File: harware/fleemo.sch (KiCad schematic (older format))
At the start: 33 parts

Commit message: add value of the components
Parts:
- C1: renamed from C?; value C_Small -> 4.7uF
- C2, C3: renamed from C?; value CP1_Small -> 10uF
- C4, C5: renamed from C?; value C_Small -> 470pF
- C6: renamed from C?; value C_Small -> 1000pF
- C7: renamed from C?; value CP1_Small -> 820uF
- C8: renamed from C?; value CP1_Small -> 680uF
- C9: renamed from C?; value C_Small -> 0.1uF
- L1: renamed from L?; value L_Small -> 220uH
- R1: renamed from R?; value R_Small -> 68
- R10: renamed from R?; value R_Small -> 330K
- R11: renamed from R?; value R_Small -> 120
- R12: renamed from R?; value R_Small -> 2
- R13: renamed from R?; value R_Small -> 20
- R14: renamed from R?; value R_Small -> 2.4k
- R2: renamed from R?; value R_Small -> 47k
- R3: renamed from R?; value R_Small -> 300k
- R4, R7: renamed from R?; value R_Small -> 100k
- R5: renamed from R?; value R_Small -> 10K
- R6: renamed from R?; value R_Small -> 220
- R8: renamed from R?; value R_Small -> 2.4
- R9: renamed from R?; value R_Small -> 22
- gave numbers to parts that had none: 9
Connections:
- no-connect marks 1 -> 2
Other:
- moved on the sheet: D1

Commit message: update sch
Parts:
- removed C4, C5: 470pF, symbol C_Small
- removed C6: 1000pF, symbol C_Small
- removed C7: 820uF, symbol CP1_Small
- removed C8: 680uF, symbol CP1_Small
- removed C9: 0.1uF, symbol C_Small
- removed D1: Diode_Bridge, symbol Diode_Bridge
- removed D2, D3, D4: D_Small, symbol D_Small
- removed P2: CONN_01X02, symbol CONN_01X02
- removed R10: 330K, symbol R_Small
- removed R11: 120, symbol R_Small
- removed R14: 2.4k, symbol R_Small
- removed R2: 47k, symbol R_Small
- removed R7: 100k, symbol R_Small
- removed R8: 2.4, symbol R_Small
- removed R9: 22, symbol R_Small
- removed U1: UCC28713, symbol UCC28713
- removed U2: 750341984, symbol 750341984
- added D1: MURS160-13-F, symbol D_Small
- added D? (x4): D_Small, symbol D_Small
- added D?: SMBJP6KE82A-TP, symbol ZENERsmall
- added U?: wurth-750312723, symbol wurth-750312723
- C1: value 4.7uF -> 1nF
- C4: renamed from C2; value 10uF -> 4.7uF
- C5: renamed from C3; value 10uF -> 4.7uF
- L1: value 220uH -> 470uH
- R1: value 68 -> 487
- R12: value 2 -> 10.0k
- R13: value 20 -> 10.0k
- R3: value 300k -> 10
- R4: value 100k -> 5.11M
- R5: value 10K -> 5.11M
- R6: value 220 -> 5.11M
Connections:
- wire segments 81 -> 39
- no-connect marks 2 -> 0
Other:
- moved on the sheet: Q1

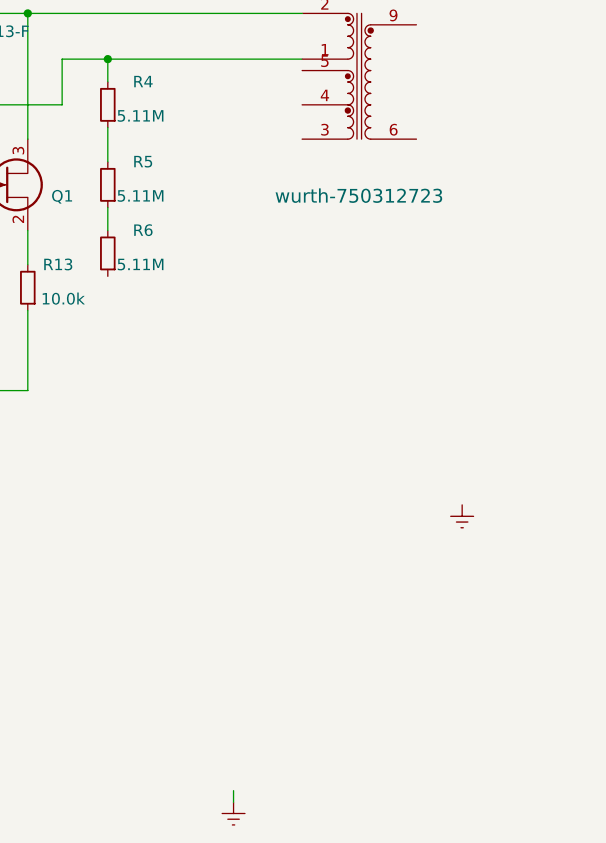
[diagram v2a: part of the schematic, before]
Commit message: edit transformer symbol
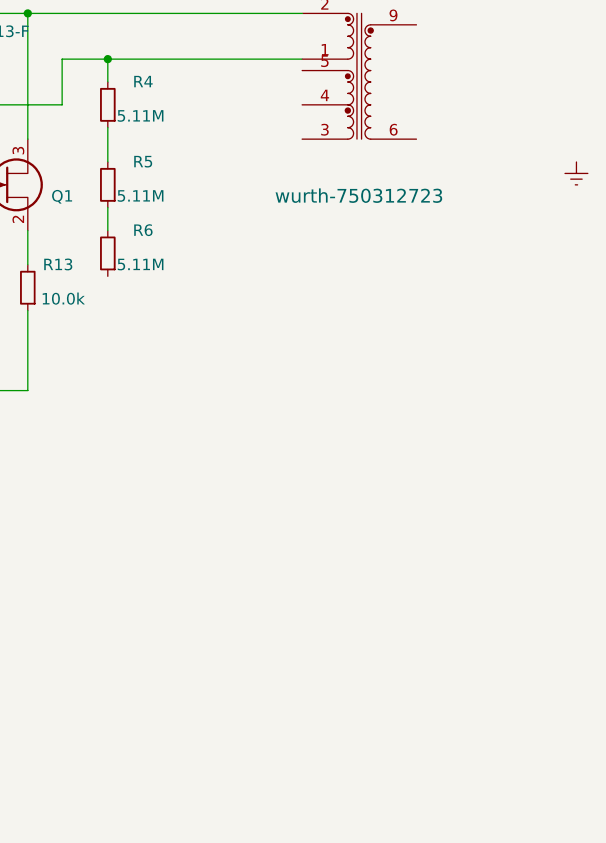
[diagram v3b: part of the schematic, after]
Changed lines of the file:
@@
-$EndComp
-$Comp
-L Earth #PWR04
-U 1 1 57871378
-P 6900 4900
-F 0 "#PWR04" H 6900 4650 50  0001 C CNN
-F 1 "Earth" H 6900 4750 50  0001 C CNN
-F 2 "" H 6900 4900 50  0000 C CNN
-F 3 "" H 6900 4900 50  0000 C CNN
-	1    6900 4900
-	1    0    0    -1
 $EndComp
 $Comp
 L Earth #PWR05
 U 1 1 578722E6
-P 7900 3600
-F 0 "#PWR05" H 7900 3350 50  0001 C CNN
-F 1 "Earth" H 7900 3450 50  0001 C CNN
-F 2 "" H 7900 3600 50  0000 C CNN
-F 3 "" H 7900 3600 50  0000 C CNN
-	1    7900 3600
+P 8400 2100
+F 0 "#PWR05" H 8400 1850 50  0001 C CNN
+F 1 "Earth" H 8400 1950 50  0001 C CNN
+F 2 "" H 8400 2100 50  0000 C CNN
+F 3 "" H 8400 2100 50  0000 C CNN
+	1    8400 2100
 	1    0    0    -1
 $EndComp
@@
 	3300 2250 4350 2250
 Wire Wire Line
-	6900 4850 6900 4900
-Wire Wire Line
 	5450 2200 5700 2200

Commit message: finish powe section
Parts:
- removed D? (x4): D_Small, symbol D_Small
- added 22.5, R11: 10, symbol R_Small
- added C2, C3: 560uF, symbol CP1_Small
- added C6, C9: np, symbol C_Small
- added C7: 330nF, symbol C_Small
- added C8: 1000pF, symbol C_Small
- added D2: np, symbol ZENERsmall
- added D3: RS1B-13-F, symbol D_Small
- added D?: Diode_Bridge, symbol Diode_Bridge
- added R10: 4.64k, symbol R_Small
- added R2: 3.01k, symbol R_Small
- added R7: 121k, symbol R_Small
- added R8: np, symbol R_Small
- added R9: 30.1k, symbol R_Small
- added U?: UCC28700, symbol UCC28700
- Q1: value Q_NJFET_GDS -> STD2HNK60Z-1
- gave numbers to parts that had none: 1
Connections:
- net Earth: now also U?.6, C2.2, C3.2, C8.1, R2.1
- net GND: now also U?.4, C6.2, C7.2, C8.2, C9.2, D?.1 (-), R8.1, R9.1, U?.5 (GND)
- net at P1.2 (P2): now also D?.2
- net at C4.1, L1.1: now also D?.3 (+)
- net at Q1.1 (G), R12.2: now also R11.2
- net at Q1.2 (D), R13.2: now also R10.1
- net at U?.5: now also D3.2 (A), R7.2
- net at U?.9: now also D2.2 (A)
- net at R3.1: now also D?.4
- net at R6.1: now also 22.5.2, C7.1, U?.2 (VDD)
- new net: R8.2, U?.1 (CBC/NTC)
- new net: R11.1, U?.3 (DRV)
- new net: C9.1, R10.2, U?.4 (CS)
- new net: C6.1, R7.1, R9.2, U?.6 (VS)
- new net: 22.5.1, D3.1 (K)
- new net: C2.1, C3.1, D2.1 (K), R2.2
- no-connect marks 0 -> 1
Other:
- moved on the sheet: D1, R1, R4, R5, R6, U?

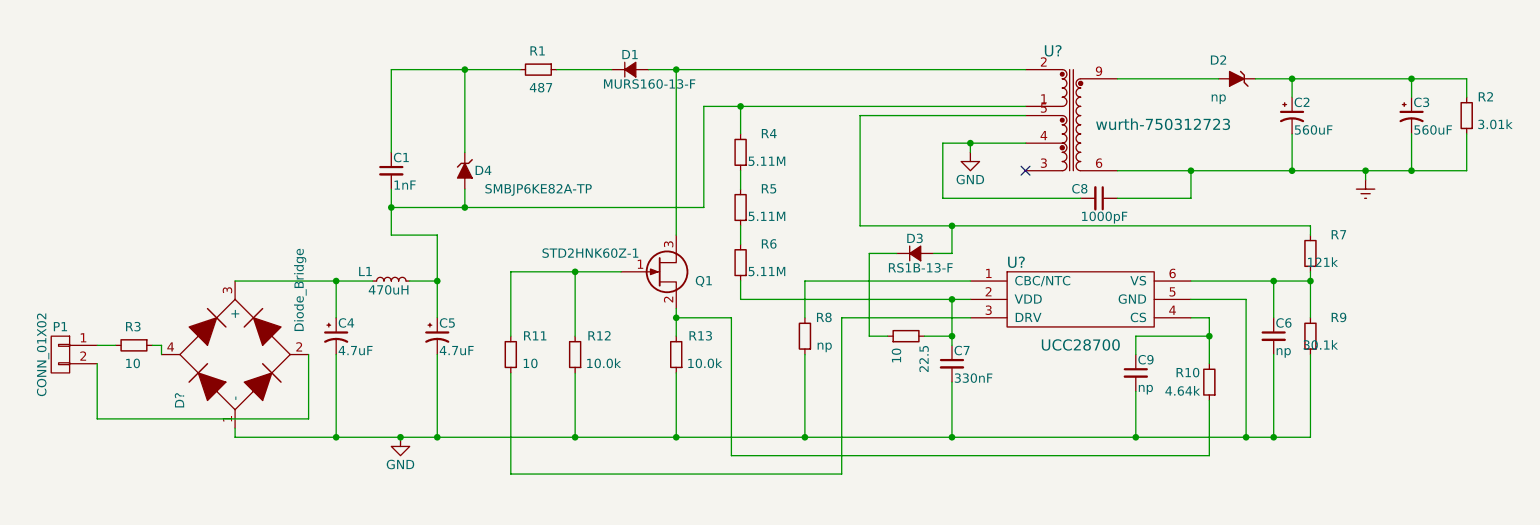
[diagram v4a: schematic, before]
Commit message: add 5v label
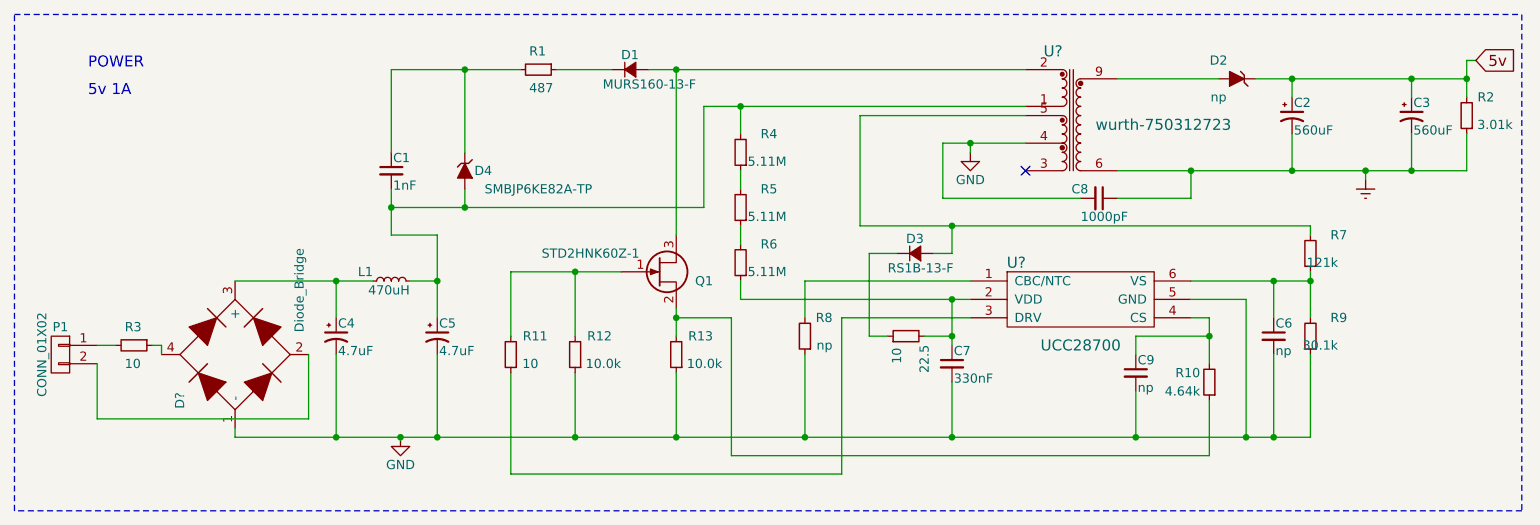
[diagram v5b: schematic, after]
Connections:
- net 5v: now reaches C2.1, C3.1, D2.1 (K), R2.2
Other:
- note added: "5v 1A\n"
- note added: "POWER"
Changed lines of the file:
@@
 	4700 3100 4700 2650
 Wire Wire Line
-	5100 2200 5700 2200
+	5100 2200 5450 2200
+Wire Wire Line
+	5450 2200 5700 2200
 Connection ~ 4500 3100
 Wire Wire Line
@@
 	4150 2250 4150 2450
 Wire Wire Line
-	4700 2000 4700 2450
+	4700 2000 4700 2250
+Wire Wire Line
+	4700 2250 4700 2450
 Wire Wire Line
 	4700 2250 4550 2250
@@
 	4450 2000 4700 2000
 Wire Wire Line
-	4450 1750 4450 2000
+	4450 1750 4450 1850
+Wire Wire Line
+	4450 1850 4450 2000
 Wire Wire Line
 	4450 1550 4450 1100
 Wire Wire Line
-	4450 1100 5150 1100
-Wire Wire Line
-	4450 1850 6150 1850
+	4450 1100 4850 1100
+Wire Wire Line
+	4850 1100 5150 1100
+Wire Wire Line
+	4450 1850 4850 1850
+Wire Wire Line
+	4850 1850 6150 1850
 Wire Wire Line
 	4850 1850 4850 1750
@@
 	5350 1100 5650 1100
 Wire Wire Line
-	5850 1100 7900 1100
+	5850 1100 6000 1100
+Wire Wire Line
+	6000 1100 7900 1100
 Wire Wire Line
 	6000 1100 6000 2000
@@
 	5450 2550 5450 2200
 Wire Wire Line
-	6000 2400 6000 2550
+	6000 2400 6000 2450
+Wire Wire Line
+	6000 2450 6000 2550
 Wire Wire Line
 	6000 3100 6000 2750
@@
 	6350 1450 6350 1300
 Wire Wire Line
-	6150 1300 7900 1300
+	6150 1300 6350 1300
+Wire Wire Line
+	6350 1300 7900 1300
 Wire Wire Line
 	6350 1650 6350 1750
@@
 	6350 2250 6350 2350
 Wire Wire Line
-	6350 2350 7600 2350
+	6350 2350 7500 2350
+Wire Wire Line
+	7500 2350 7600 2350
 Wire Wire Line
 	5100 2550 5100 2200
@@
 	7000 1350 7000 1950
 Wire Wire Line
-	7000 1950 9450 1950
+	7000 1950 7500 1950
+Wire Wire Line
+	7500 1950 9450 1950
 Wire Wire Line
 	9450 1950 9450 2000
 Wire Wire Line
-	9450 2200 9450 2450
+	9450 2200 9450 2250
+Wire Wire Line
+	9450 2250 9450 2450
 Wire Wire Line
 	9450 3100 9450 2650
@@
 $EndComp
 Wire Wire Line
-	7500 2350 7500 2600
+	7500 2350 7500 2550
+Wire Wire Line
+	7500 2550 7500 2600
 Connection ~ 7500 2350
 Wire Wire Line
@@
 Connection ~ 7500 1950
 Wire Wire Line
-	8800 2250 9450 2250
+	8800 2250 9250 2250
+Wire Wire Line
+	9250 2250 9450 2250
 Connection ~ 9450 2250
 $Comp
@@
 	8800 2450 8900 2450
 Wire Wire Line
-	8900 2450 8900 2700
+	8900 2450 8900 2550
+Wire Wire Line
+	8900 2550 8900 2700
 Wire Wire Line
 	8900 2900 8900 3200
@@
 $EndComp
 Wire Wire Line
-	9150 1150 10300 1150
+	9150 1150 9350 1150
+Wire Wire Line
+	9350 1150 10000 1150
+Wire Wire Line
+	10000 1150 10300 1150
 Wire Wire Line
 	9350 1150 9350 1250
 Wire Wire Line
-	8400 1650 10300 1650
+	8400 1650 8800 1650
+Wire Wire Line
+	8800 1650 9350 1650
+Wire Wire Line
+	9350 1650 9750 1650
+Wire Wire Line
+	9750 1650 10000 1650
+Wire Wire Line
+	10000 1650 10300 1650
 Wire Wire Line
 	9350 1650 9350 1450
@@
 $EndComp
 Wire Wire Line
+	10300 1050 10300 1150
+Wire Wire Line
 	10300 1150 10300 1250
 Connection ~ 10000 1150
@@
 $EndComp
 Wire Wire Line
-	7900 1500 7450 1500
+	7900 1500 7600 1500
+Wire Wire Line
+	7600 1500 7450 1500
 Wire Wire Line
 	7450 1500 7450 1800
@@
 $EndComp
 Wire Wire Line
-	3600 2250 4350 2250
-Wire Wire Line
-	3600 3100 9450 3100
+	3600 2250 4150 2250
+Wire Wire Line
+	4150 2250 4350 2250
+Wire Wire Line
+	3600 3100 4150 3100
+Wire Wire Line
+	4150 3100 4500 3100
+Wire Wire Line
+	4500 3100 4700 3100
+Wire Wire Line
+	4700 3100 5450 3100
+Wire Wire Line
+	5450 3100 6000 3100
+Wire Wire Line
+	6000 3100 6700 3100
+Wire Wire Line
+	6700 3100 7500 3100
+Wire Wire Line
+	7500 3100 8500 3100
+Wire Wire Line
+	8500 3100 9100 3100
+Wire Wire Line
+	9100 3100 9250 3100
+Wire Wire Line
+	9250 3100 9450 3100
 Wire Wire Line
 	3600 3100 3600 3050
@@
 Wire Wire Line
 	4000 3000 4000 2650
+Text GLabel 10350 1050 2    60   Input ~ 0
+5v
+Wire Wire Line
+	10350 1050 10300 1050
+Connection ~ 10300 1150
+Wire Notes Line
+	2400 800  10600 800
+Wire Notes Line
+	10600 800  10600 3500
+Wire Notes Line
+	10600 3500 2400 3500
+Wire Notes Line
+	2400 3500 2400 800
+Text Notes 2800 1100 0    60   ~ 0
+POWER
+Text Notes 2800 1250 0    60   ~ 0
+5v 1A\n
 $EndSCHEMATC
